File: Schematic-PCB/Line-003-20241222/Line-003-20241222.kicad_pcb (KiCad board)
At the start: 4 copper layers, 196 x 193.6 mm, 244 parts, among them J1 VIN, J2 Conn_MD, U47 LM393, U48 LM393, U49 LM393, U50 LM393, U51 LM393, U52 LM393, U53 LM393, U54 LM393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

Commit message: update: とりあえずラインセンサ基板の配線を終わらせた
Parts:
- moved C18 6.55 mm to (-82.8, 16.6), turned to 0 degrees
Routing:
- net Th2: track 14.8 -> 354.8 mm, vias 5 -> 10
- net Line-R: track 71.4 -> 296.7 mm, vias 1 -> 6
- net Line19: track 9.40 -> 189.6 mm, vias 1 -> 4
- net Line21: track 8.97 -> 175.8 mm, vias 0 -> 1
- net Line23: track 8.97 -> 148.6 mm, vias 1 -> 2
- net Th: track 152.1 -> 189.4 mm, vias 31 -> 34
- net +5V: track 118.0 -> 135.1 mm, vias 52 -> 55
- net GND: track 0.00 -> 16.1 mm, vias 10 -> 15
- net Line-F: track 190.0 -> 184.2 mm
- net Line01: track 119.5 -> 115.6 mm
- net 18: track 143.7 -> 146.4 mm, vias 2 -> 4
- net RESET: track 0.00 -> 1.73 mm
- net 17: track 116.6 -> 118.1 mm, vias 2 -> 4
- net 16: track 117.4 -> 118.9 mm, vias 2 -> 4
- net 09: track 15.8 -> 16.7 mm
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
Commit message: update: ラインセンサ基板の1次DRを完了させ、発注用ファイルを出力した
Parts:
- added C20: 1000uF, Capacitor_THT:CP_Radial_D10.0mm_P5.00mm, F.Cu at (-12.0, 50.4)
- added SW1: RESET, @2024TOINIOT2-Line:Tactile1, B.Cu at (-84.5, 9.60)
- U47, U48, U49, U50, U51, U52, U53, U54, U55, U56, U57, U58, U59, U60, U61: footprint Package_SO:SOIC-8_3.9x4.9mm_P1.27mm -> Package_SO:SOP-8_3.9x4.9mm_P1.27mm
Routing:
- net RESET: track 1.73 -> 12.9 mm
- net Line21: track 175.8 -> 176.9 mm
- net Th: track 189.4 -> 190.1 mm
- net Line23: track 148.6 -> 149.1 mm, vias 2 -> 1
- net GND: vias 15 -> 18
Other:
- outline, holes or cut-outs redrawn
- board text added: "RST"

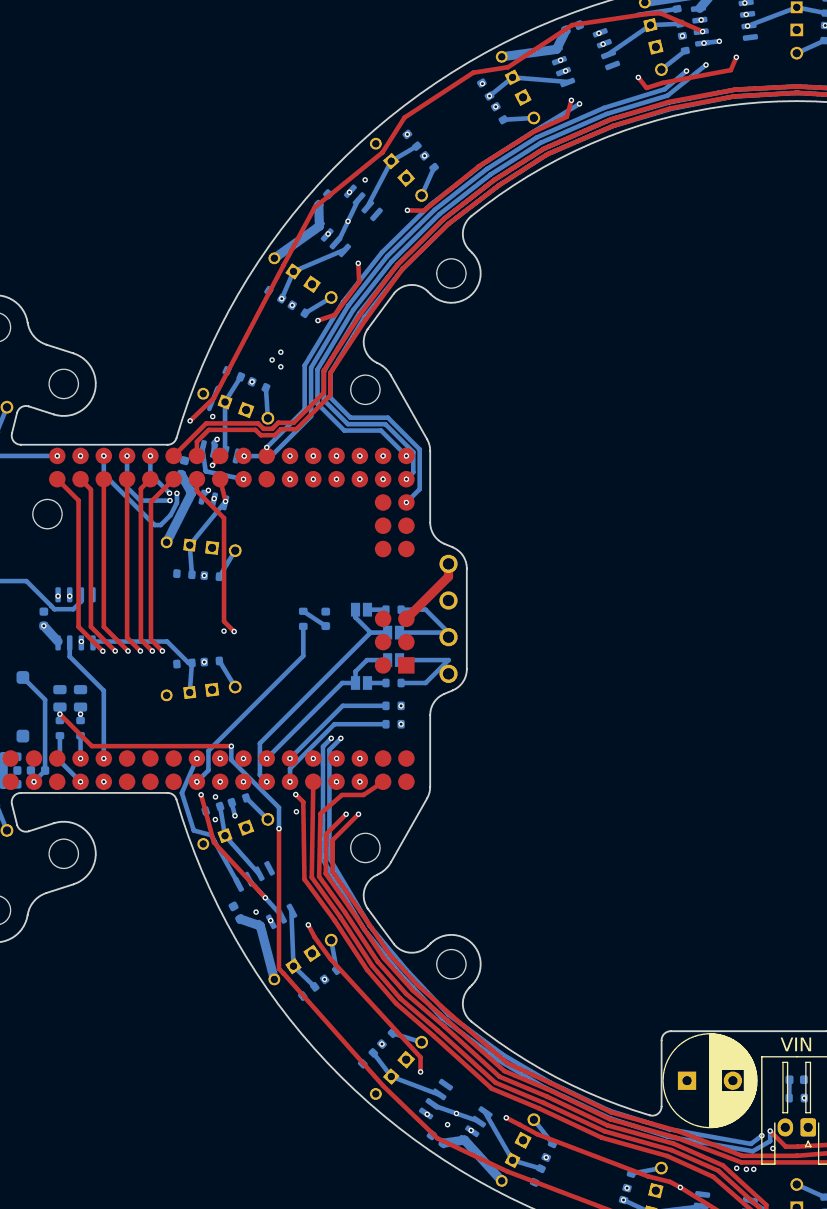
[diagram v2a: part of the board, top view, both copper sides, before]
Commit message: update: ラインセンサ基板の2次DRを完了させた
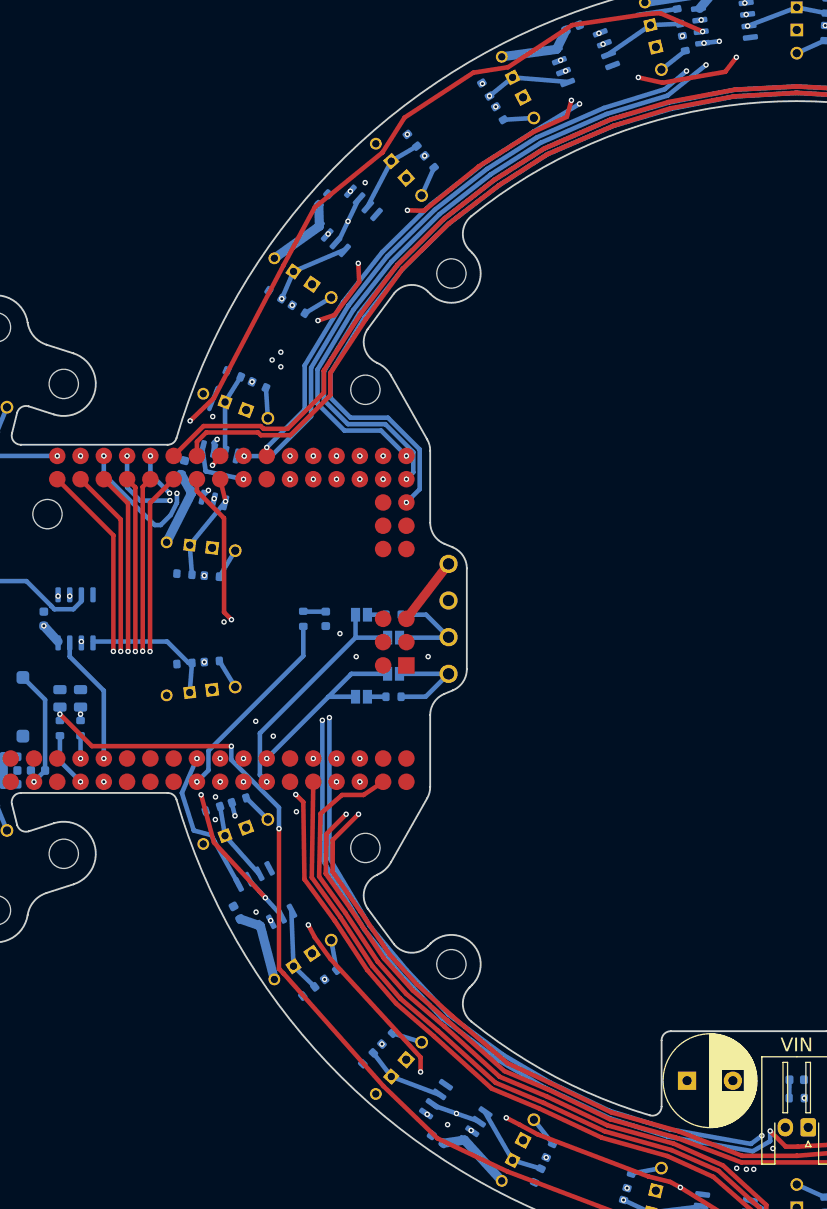
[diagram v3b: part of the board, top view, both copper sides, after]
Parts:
- removed R77, R78: 1K, Resistor_SMD:R_0603_1608Metric
- moved JP10 1.50 mm to (-47.5, 8.50)
- moved JP8 1.50 mm to (-44.0, 6.00)
- moved R87 1.50 mm to (-44.0, 8.50)
- moved JP7 0.55 mm to (-44.0, 2.05)
- moved JP9 0.55 mm to (-47.5, -0.45)
- moved R86 0.55 mm to (-44.0, -0.45)
- turned D47 to 90 degrees
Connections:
- U62 pad D20: SDA -> unconnected-(U62-PadD20)
- U62 pad D21: SCL -> unconnected-(U62-PadD21)
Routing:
- net SCL: track 13.9 -> 0.00 mm, vias 1 -> 0
- net SDA: track 12.9 -> 0.00 mm, vias 1 -> 0
- net Line-F: track 184.2 -> 180.0 mm
- net 04: track 36.9 -> 34.2 mm
- net Line01: track 115.6 -> 114.0 mm
- net TX: track 18.4 -> 20.0 mm
- net Line13: track 117.2 -> 116.1 mm
- net Line19: track 189.6 -> 188.5 mm
- net 20: track 183.7 -> 182.8 mm
- net 21: track 165.0 -> 164.2 mm
- net Line03: track 83.5 -> 82.7 mm
- net 22: track 154.6 -> 153.8 mm
- net Line-R: track 296.7 -> 296.0 mm
- net Th: track 190.1 -> 189.4 mm
- net Line17: track 184.3 -> 183.7 mm
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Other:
- board text added: "+5V"
- board text added: "GND"
- board text removed: "+"
- board text removed: "G"
